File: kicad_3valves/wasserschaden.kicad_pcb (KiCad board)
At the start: 2 copper layers, 50 x 50 mm, 30 parts, among them J1 v1 out, J2 12V in, J3 sense, J4 v2 out, J5 v3 out, U1 stepdown, U2 WeMos_mini, U3 DS18B20

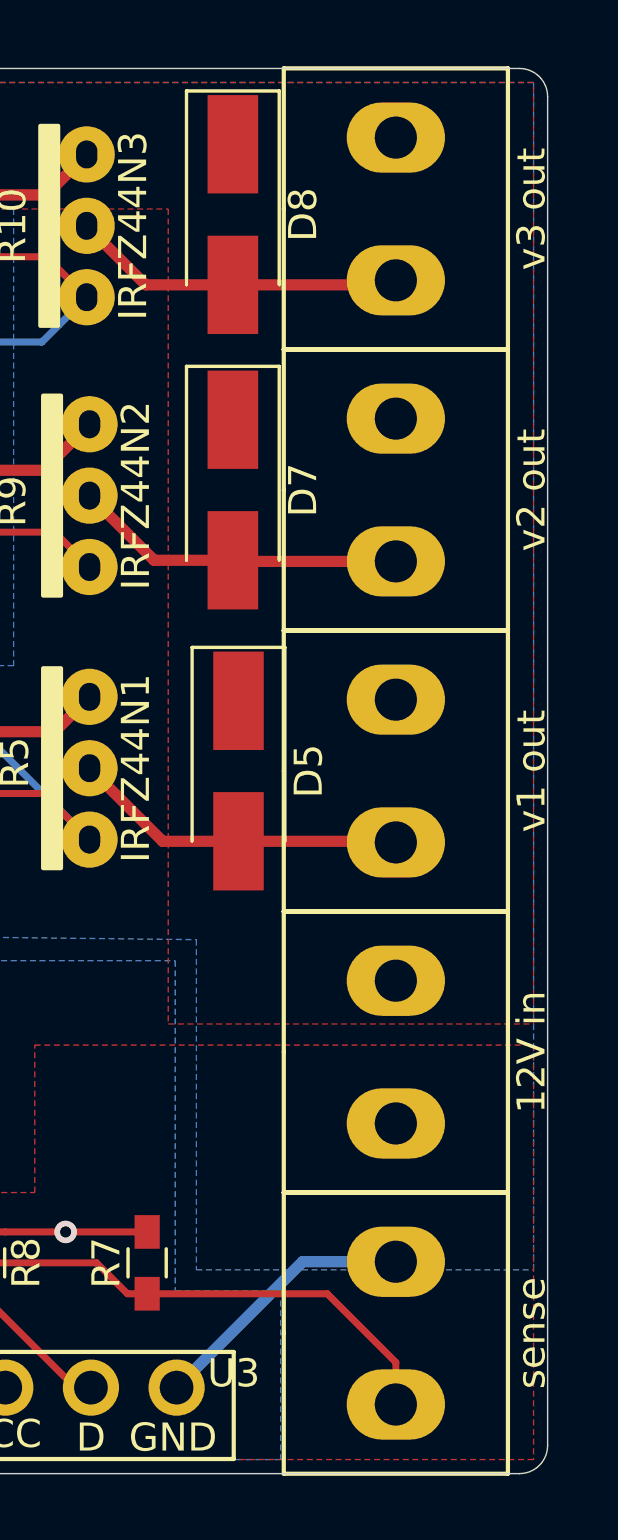
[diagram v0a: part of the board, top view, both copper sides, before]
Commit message: fixed terminal spacing
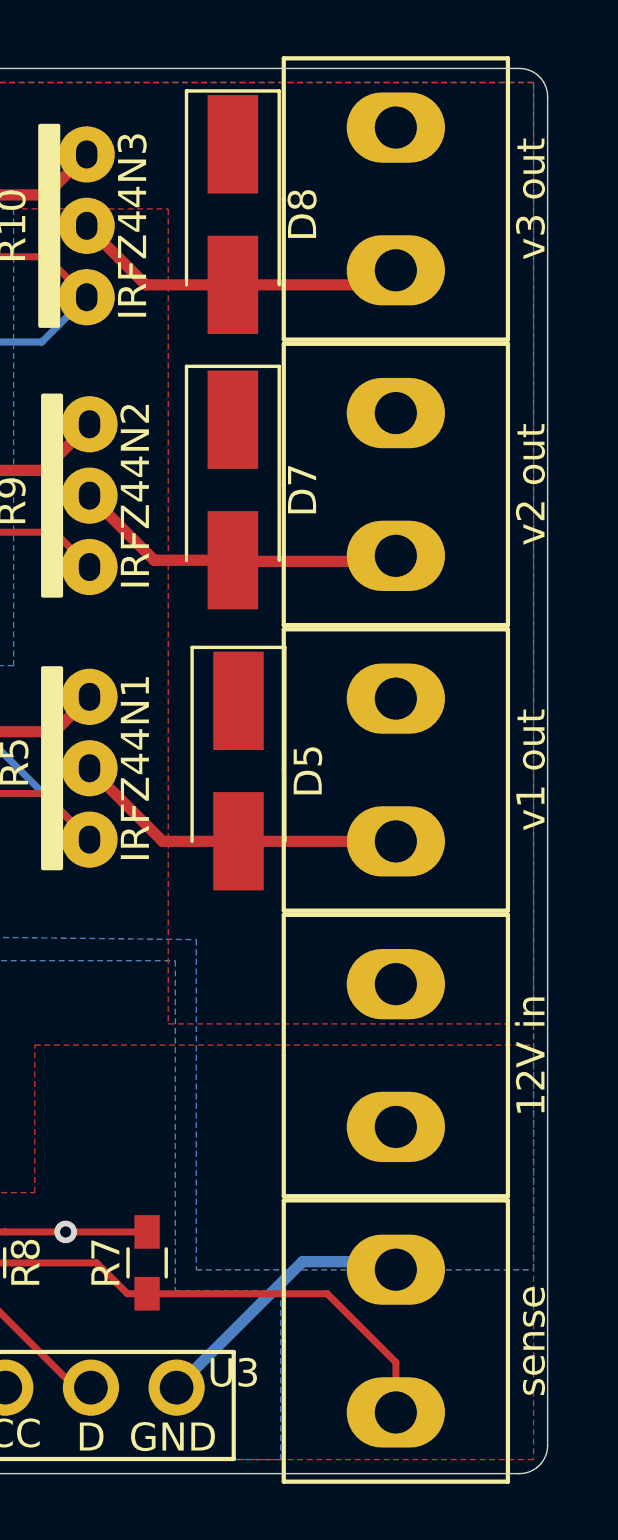
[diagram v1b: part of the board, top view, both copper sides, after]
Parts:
- moved J5 0.36 mm to (109.6, 64.6)
- moved J3 0.28 mm to (109.6, 105.3)
- moved J4 0.20 mm to (109.6, 74.8)
- moved J2 0.12 mm to (109.6, 95.1)
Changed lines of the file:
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@@
   )
   (module custom:termina_2pin (layer F.Cu)
-    (at 109.6 65 90)
+    (at 109.6 64.643 90)
     (fp_text reference J5 (at 0 2.54 90) (layer F.Fab)
       (effects (font (size 1 1) (thickness 0.15)))
@@
   )
   (module custom:termina_2pin (layer F.Cu)
-    (at 109.6 75 90)
+    (at 109.6 74.803 90)
     (fp_text reference J4 (at 0 2.54 90) (layer F.Fab)
       (effects (font (size 1 1) (thickness 0.15)))
@@
   )
   (module custom:termina_2pin (layer F.Cu)
-    (at 109.6 105 90)
+    (at 109.6 105.283 90)
     (fp_text reference J3 (at 0 2.54 90) (layer F.Fab)
       (effects (font (size 1 1) (thickness 0.15)))
@@
   )
   (module custom:termina_2pin (layer F.Cu)
-    (at 109.6 95 90)
+    (at 109.6 95.123 90)
     (fp_text reference J2 (at 0 2.54 90) (layer F.Fab)
       (effects (font (size 1 1) (thickness 0.15)))
@@
   )
   (module custom:termina_2pin (layer F.Cu)
-    (at 109.6 85 90)
+    (at 109.6 84.963 90)
     (fp_text reference J1 (at 0 2.54 90) (layer F.Fab)
       (effects (font (size 1 1) (thickness 0.15)))

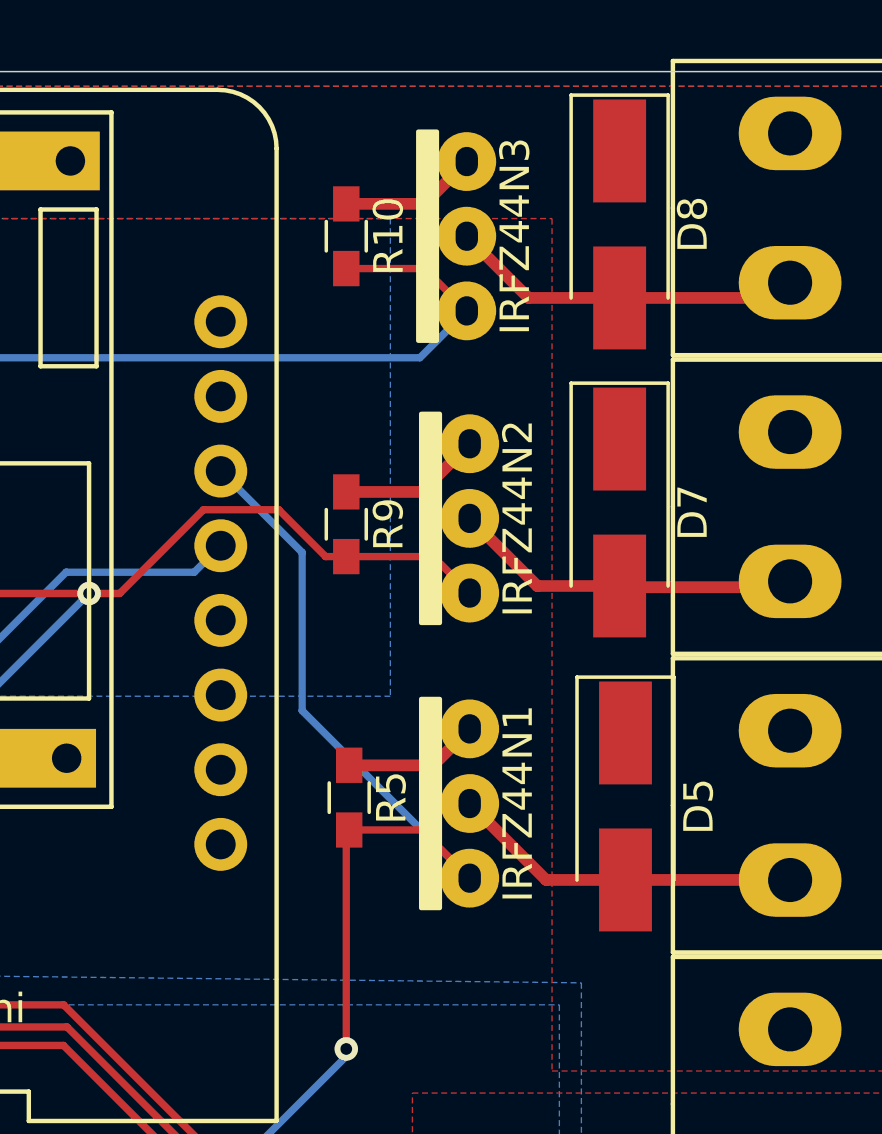
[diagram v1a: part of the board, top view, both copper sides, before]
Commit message: use propper symbol and footprint for irlz44n
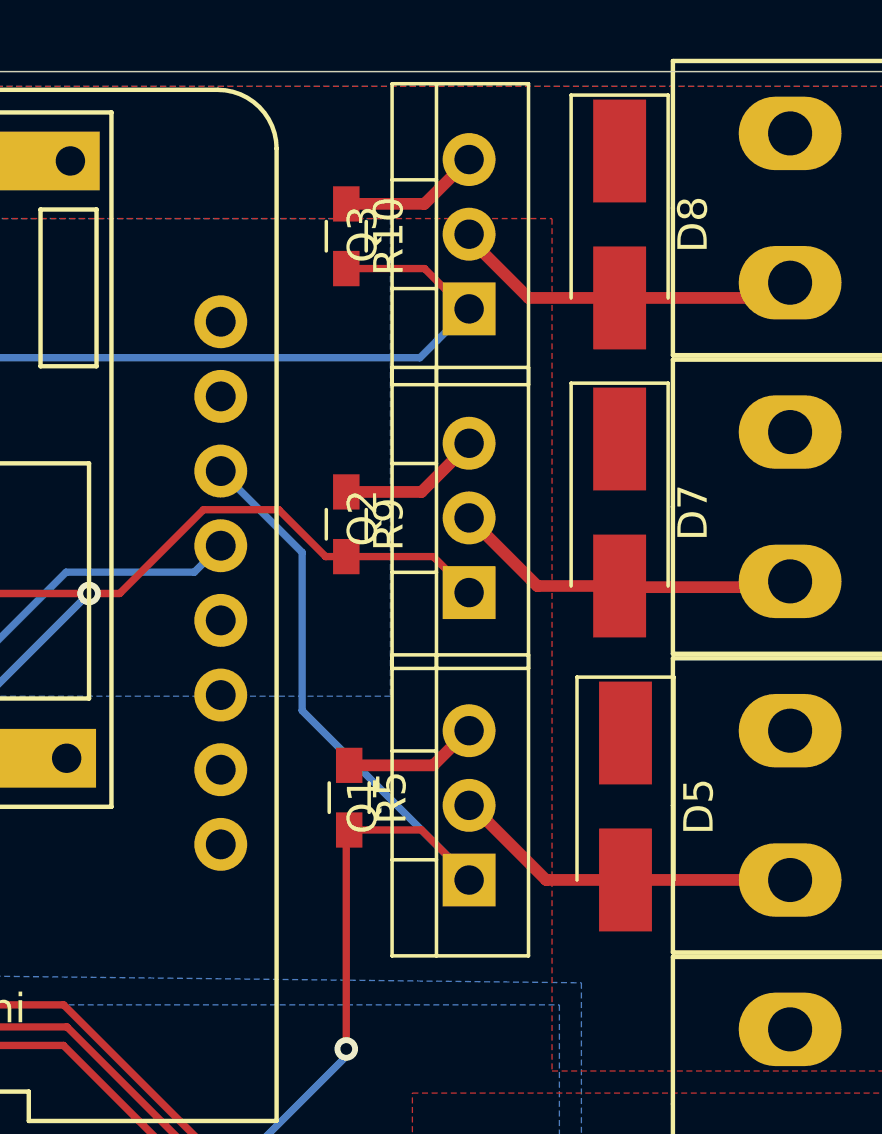
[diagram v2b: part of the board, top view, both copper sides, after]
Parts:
- removed IRFZ44N1, IRFZ44N2, IRFZ44N3: , custom:irlz44n_vertical
- added Q1: IRLZ44N, TO_SOT_Packages_THT:TO-220-3_Vertical, F.Cu at (98.7, 87.5)
- added Q2: IRLZ44N, TO_SOT_Packages_THT:TO-220-3_Vertical, F.Cu at (98.7, 77.7)
- added Q3: IRLZ44N, TO_SOT_Packages_THT:TO-220-3_Vertical, F.Cu at (98.7, 68.1)
